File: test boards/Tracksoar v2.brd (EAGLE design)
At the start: 50.4 x 19.5 mm, 37 parts, among them IC1 BME280, IC2 74AHC1G125DBV, Y1 16MHZ

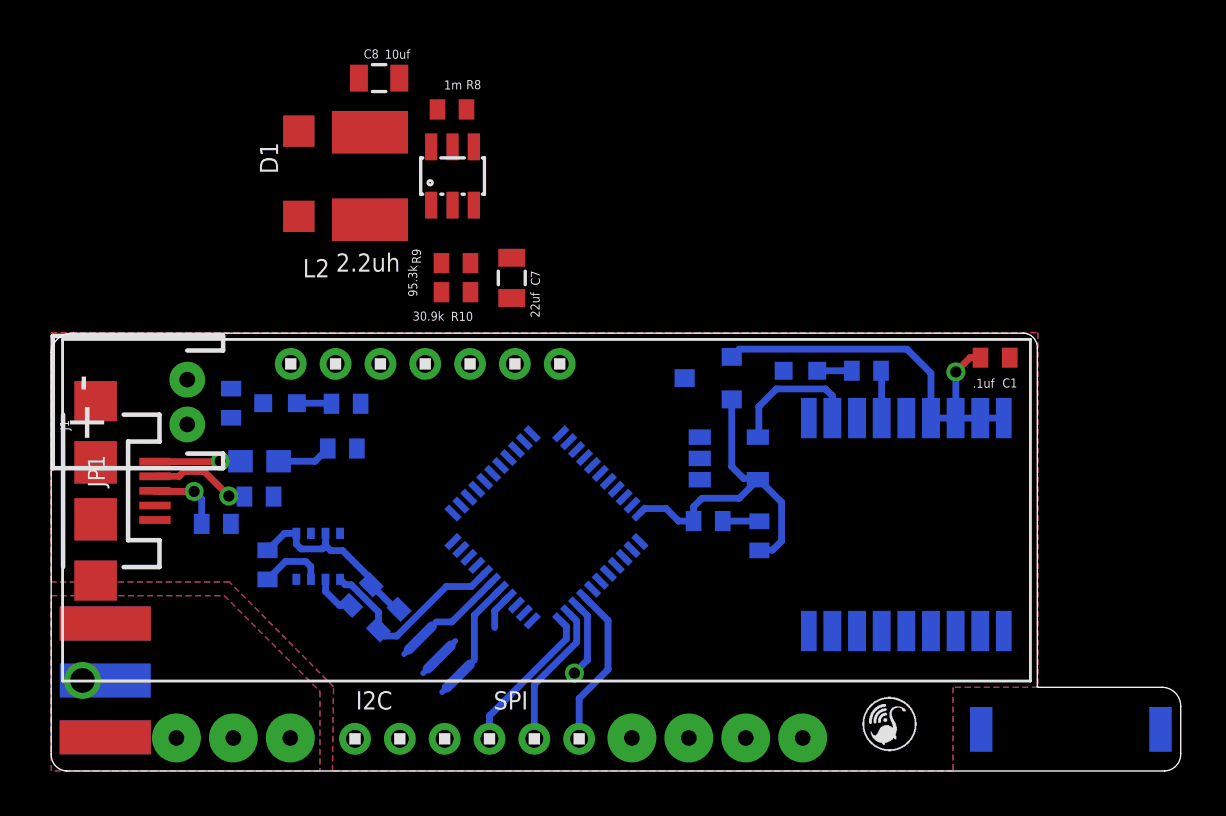
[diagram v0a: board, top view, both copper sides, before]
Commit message: Removed v1.1 headers
removed the v1.1 headers to simplify layout.
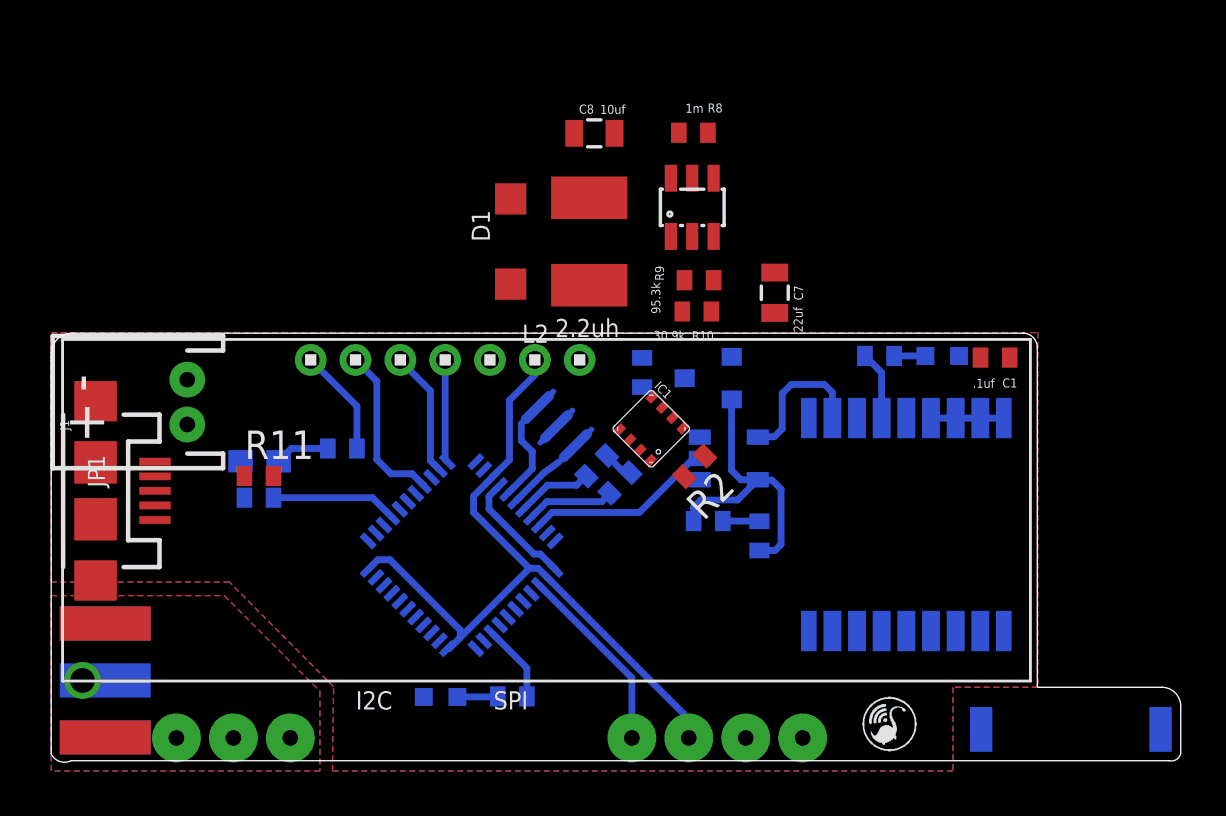
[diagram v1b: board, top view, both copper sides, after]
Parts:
- removed SPI/I2C: 1X6, headers(2mm):1X6
- moved R2 19.6 mm to (28.7, 13.6), flipped to the top, turned to 225 degrees
- moved C2 18.4 mm to (26.4, 17.8), turned to 90 degrees
- moved IC1 15.9 mm to (26.8, 15.3), flipped to the top, turned to 315 degrees
- moved R6 15.0 mm to (20.6, 3.35)
- moved PTT 14.9 mm to (17.4, 3.33)
- moved R3 12.6 mm to (25.4, 12.9)
- moved C7 11.8 mm to (32.3, 21.4)
- moved Y1 11.5 mm to (22.6, 15.4), turned to 45 degrees
- moved R7 11.5 mm to (24.4, 13.6)
- moved R9 10.9 mm to (28.9, 21.9)
- moved R8 10.8 mm to (28.7, 28.5)
- moved LT3426 10.8 mm to (28.6, 25.2)
- moved R10 10.8 mm to (28.8, 20.5)
- moved L2 10.2 mm to (24.0, 23.6)
- moved D1 9.92 mm to (20.5, 23.6)
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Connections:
- removed net DTR: FTDI.6
- net GND: no longer FTDI.2
- net MISO: now also FTDI.4; no longer SPI/I2C.4
- net MOSI: now also FTDI.5; no longer SPI/I2C.5
- net RX: no longer FTDI.4
- net SCK: now also FTDI.3; no longer SPI/I2C.3
- net SCL: no longer SPI/I2C.1
- net SDA: no longer SPI/I2C.2
- net SS: now also FTDI.6; no longer SPI/I2C.6
- net TX: no longer FTDI.5
- net VCC: now also FTDI.2; no longer FTDI.3
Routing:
- net VCC: track 17.9 -> 49.0 mm
- net 3V: track 26.8 -> 4.61 mm, vias 1 -> 0
- net SCK: track 11.0 -> 0.00 mm, vias 1 -> 0
- net D4: track 0.00 -> 8.52 mm
- net TX: track 0.00 -> 8.39 mm
- net SCL: track 9.13 -> 3.41 mm
- net D+: track 0.00 -> 5.64 mm
- net !RESET: track 0.00 -> 4.81 mm
- net N$7: track 4.54 -> 0.00 mm, vias 1 -> 0
- net N$14: track 3.82 -> 0.00 mm, vias 1 -> 0
- net GND: track 3.25 -> 6.97 mm
- net LED: track 0.00 -> 3.48 mm
- net N$8: track 3.34 -> 0.00 mm, vias 1 -> 0
- net N$2: track 2.93 -> 0.00 mm
- net MISO: track 6.79 -> 4.58 mm
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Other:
- board size 50.4 x 19.5 mm -> 50.4 x 19.1 mm

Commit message: Tracksoar v2 rev2
finalized routing, added 3v access to programming header
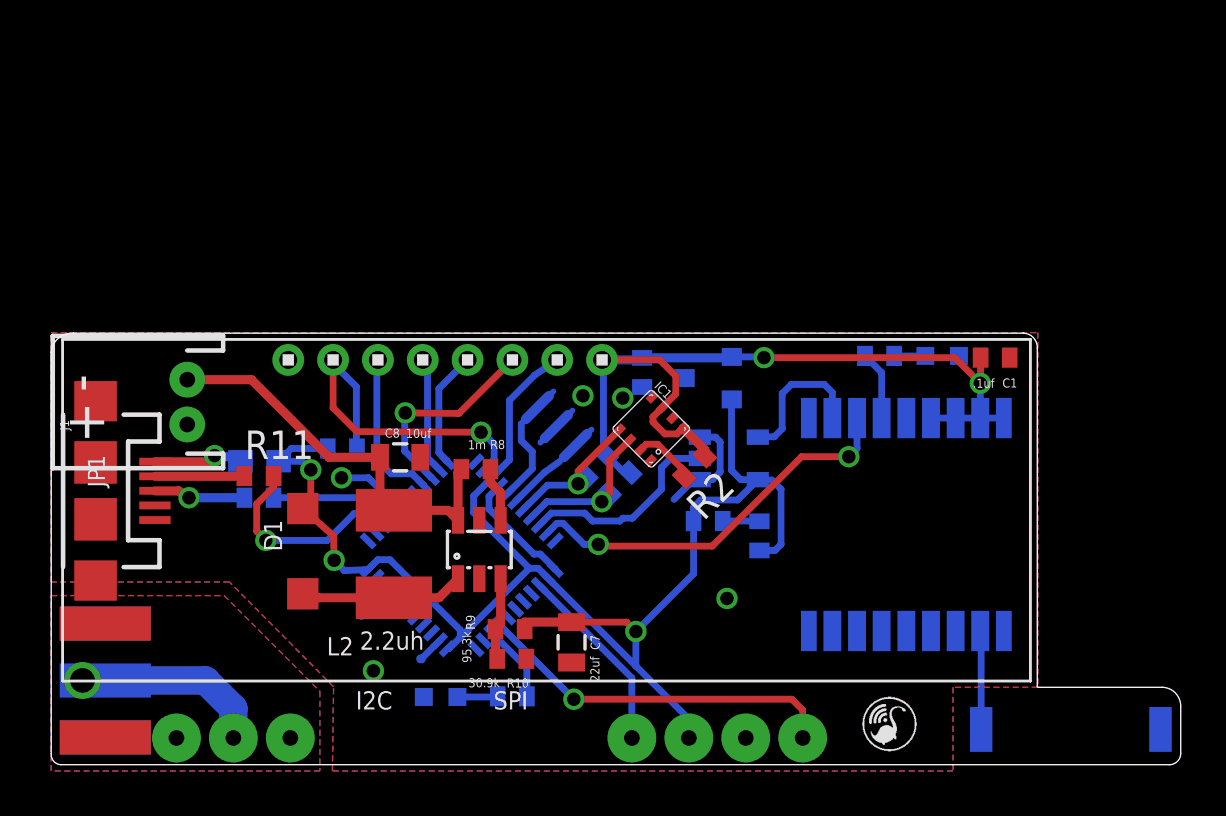
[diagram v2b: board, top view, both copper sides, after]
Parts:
- FTDI: value 1X7 -> 1X8; device headers(2mm):1X7 -> headers(2mm):1X8
- moved C7 18.0 mm to (23.2, 5.77)
- moved LT3426 18.0 mm to (19.1, 9.91)
- moved R8 17.9 mm to (19.0, 13.5)
- moved R9 17.7 mm to (20.5, 6.35)
- moved R10 17.6 mm to (20.6, 5.03)
- moved C8 16.8 mm to (15.6, 14.0)
- moved D1 16.6 mm to (11.3, 9.83)
- moved L2 16.4 mm to (15.3, 9.70)
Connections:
- net 3V: now also FTDI.1
- net GND: now also FTDI.8; no longer FTDI.1
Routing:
- net 3V: track 4.61 -> 38.4 mm, vias 0 -> 2
- net VCC: track 49.0 -> 70.7 mm, vias 0 -> 3
- net 15V: track 0.00 -> 18.0 mm
- net RX: track 0.00 -> 17.6 mm, vias 0 -> 2
- net D3: track 0.00 -> 16.3 mm, vias 0 -> 1
- net GND: track 6.97 -> 18.3 mm, vias 0 -> 5
- net !RESET: track 4.81 -> 15.7 mm, vias 0 -> 1
- net D-: track 0.00 -> 9.42 mm, vias 0 -> 1
- net SCK: track 0.00 -> 9.18 mm, vias 0 -> 1
- net N$1: track 0.00 -> 7.55 mm
- net N$9: track 0.00 -> 7.30 mm
- net N$6: track 0.00 -> 4.41 mm
- net N$8: track 0.00 -> 4.08 mm, vias 0 -> 1
- net N$14: track 0.00 -> 4.04 mm, vias 0 -> 1
- net N$7: track 0.00 -> 3.99 mm
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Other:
- board size 50.4 x 19.1 mm -> 50.4 x 19.3 mm

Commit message: tracksoar v2 rev3
added GPIO and analog pins to new header with i2c.
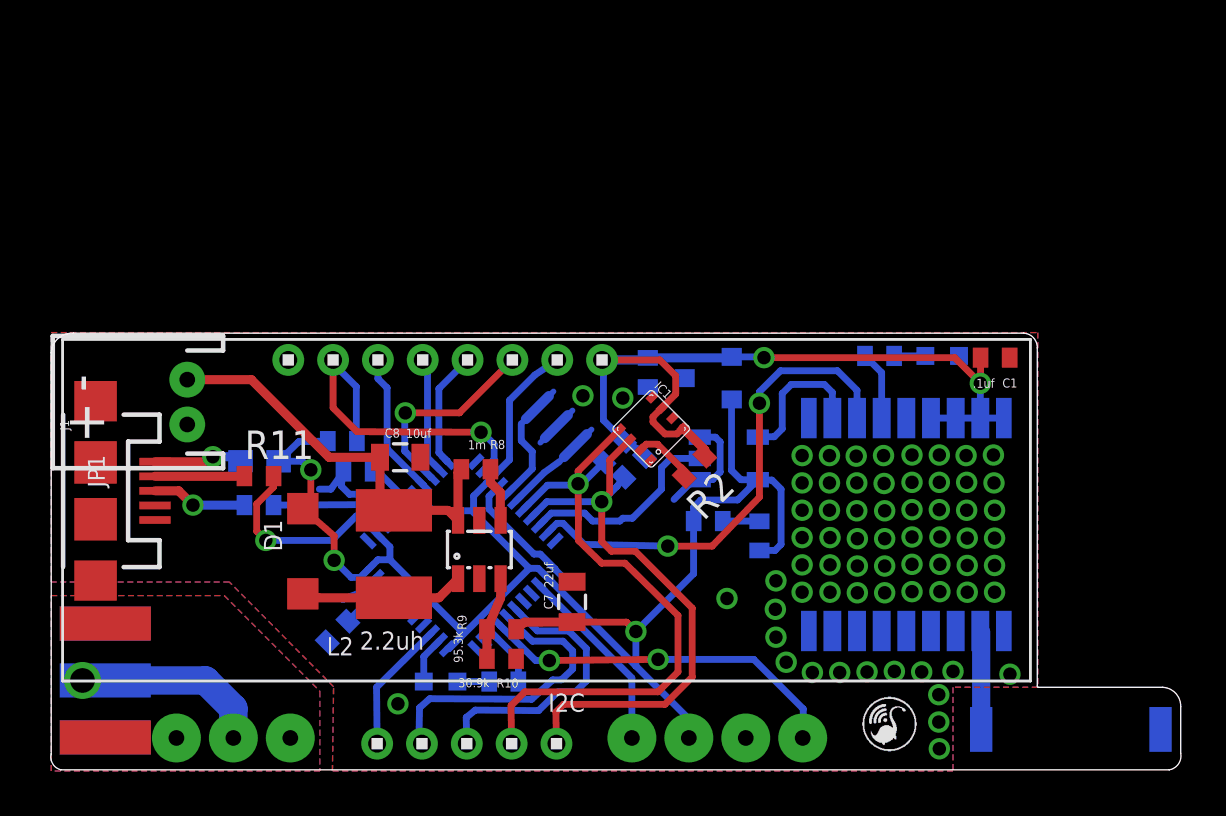
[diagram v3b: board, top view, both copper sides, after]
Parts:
- added C5, C6: 22uf, rcl:C0402
- added U$3: 1X5, headers(2mm):1X5
- moved C7 1.80 mm to (23.3, 7.57), turned to 90 degrees
- moved R7 1.01 mm to (25.1, 14.3)
- moved R3 0.95 mm to (26.0, 13.6)
- moved R6 0.76 mm to (20.2, 4.01)
- moved PTT 0.69 mm to (17.4, 4.01)
- moved R10 0.46 mm to (20.1, 5.03)
- moved R9 0.38 mm to (20.1, 6.35)
- moved R4 0.33 mm to (9.30, 11.9)
- moved R5 0.33 mm to (13.0, 14.7)
- moved C2 0.25 mm to (26.6, 17.8)
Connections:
- new net A0: U$3.1, U$4.36
- new net D13: U$4.32
- new net D8: U$3.3, U$4.28
- new net D9: U$3.2, U$4.29
- new net N$17: C6.2, U$4.42
- new net N$20: C5.2, U$4.6
- net GND: now also C5.1, C6.1
- net SCL: now also U$3.4
- net SDA: now also U$3.5
- net VCC: now also U$4.2, U$4.7
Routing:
- net SCL: track 6.60 -> 28.2 mm
- net SDA: track 7.22 -> 26.4 mm
- net D9: track 0.00 -> 13.5 mm
- net D8: track 0.00 -> 12.5 mm
- net A0: track 0.00 -> 5.97 mm
- net VCC: track 70.7 -> 75.6 mm
- net RX: track 17.6 -> 22.0 mm
- net GND: track 18.3 -> 21.0 mm, vias 5 -> 66
- net N$17: track 0.00 -> 2.28 mm
- net N$20: track 0.00 -> 2.11 mm
- net LED: track 3.48 -> 2.67 mm
- net 3V: track 38.4 -> 37.9 mm
- net SS: track 7.04 -> 6.51 mm
- net D3: track 16.3 -> 16.4 mm, vias 1 -> 2
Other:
- board size 50.4 x 19.3 mm -> 50.4 x 19.5 mm
- board text added: "Tracksoar v2"
- board text removed: "FTDI"
- board text removed: "Tracksoar v1.1"
